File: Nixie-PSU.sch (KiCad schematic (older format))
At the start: 17 parts, among them J1 Conn_Mains, J2 Conn_Pwr_Out, Q1 MJE18008-D

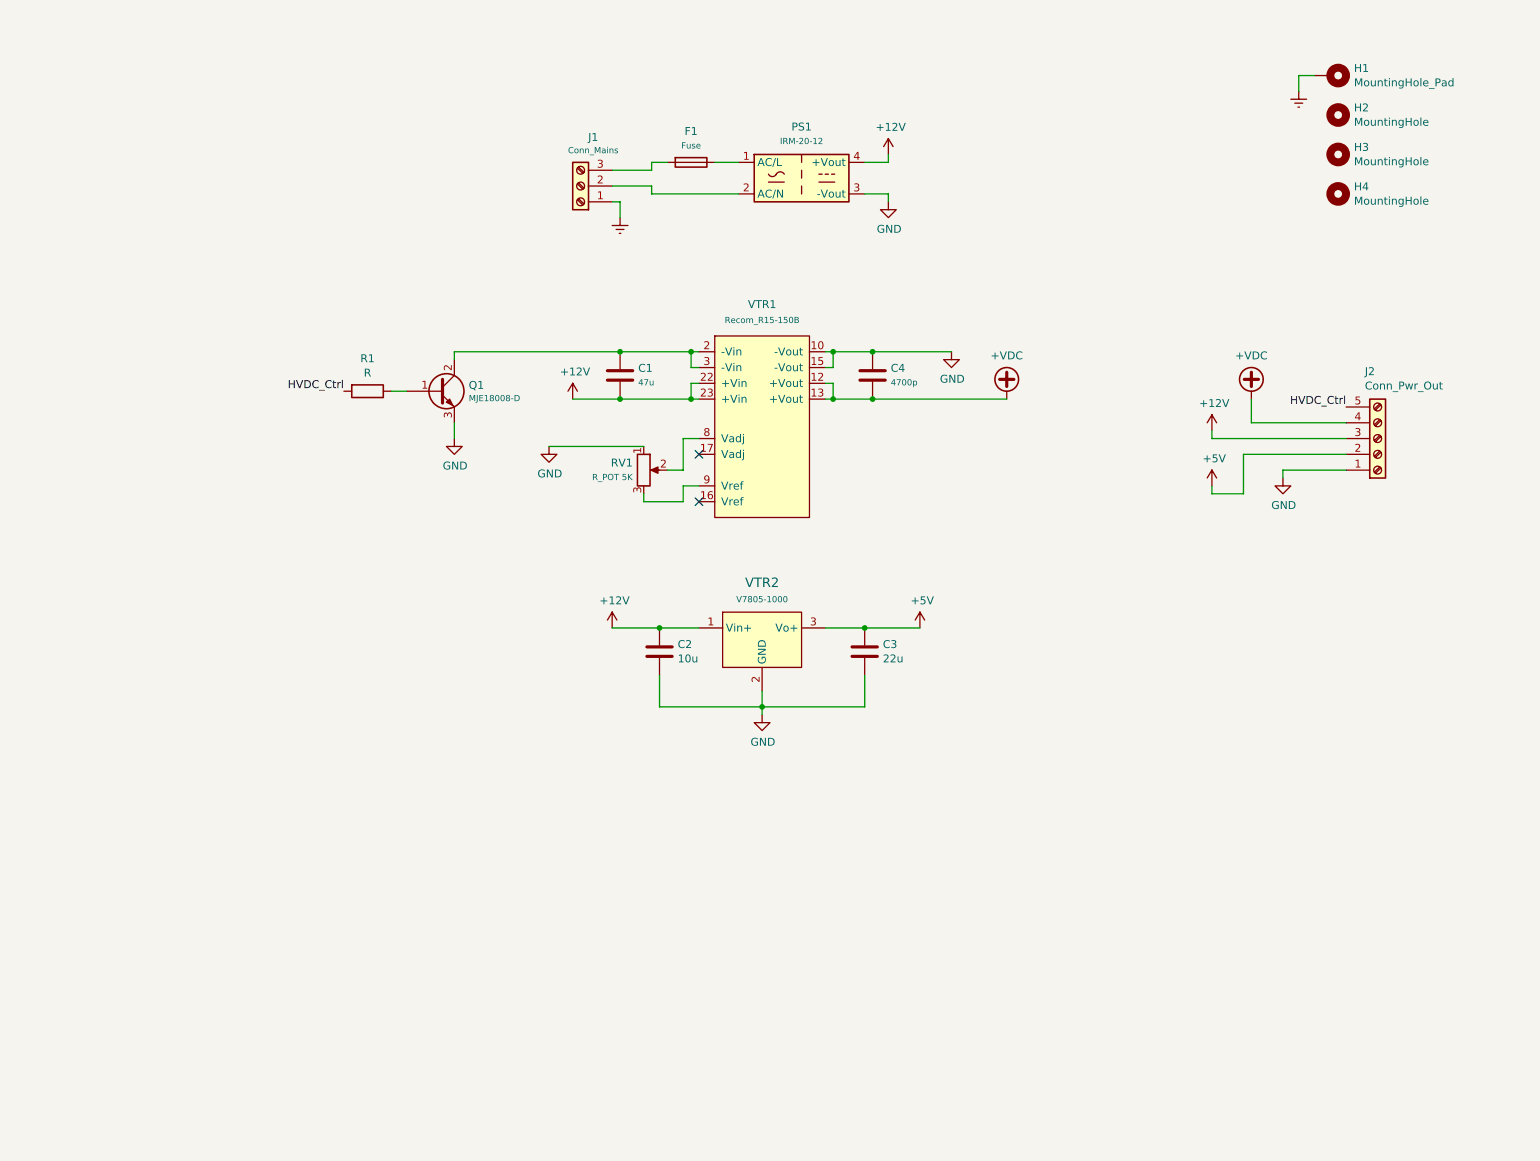
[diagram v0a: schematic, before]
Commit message: Cleaned-up docs slightly
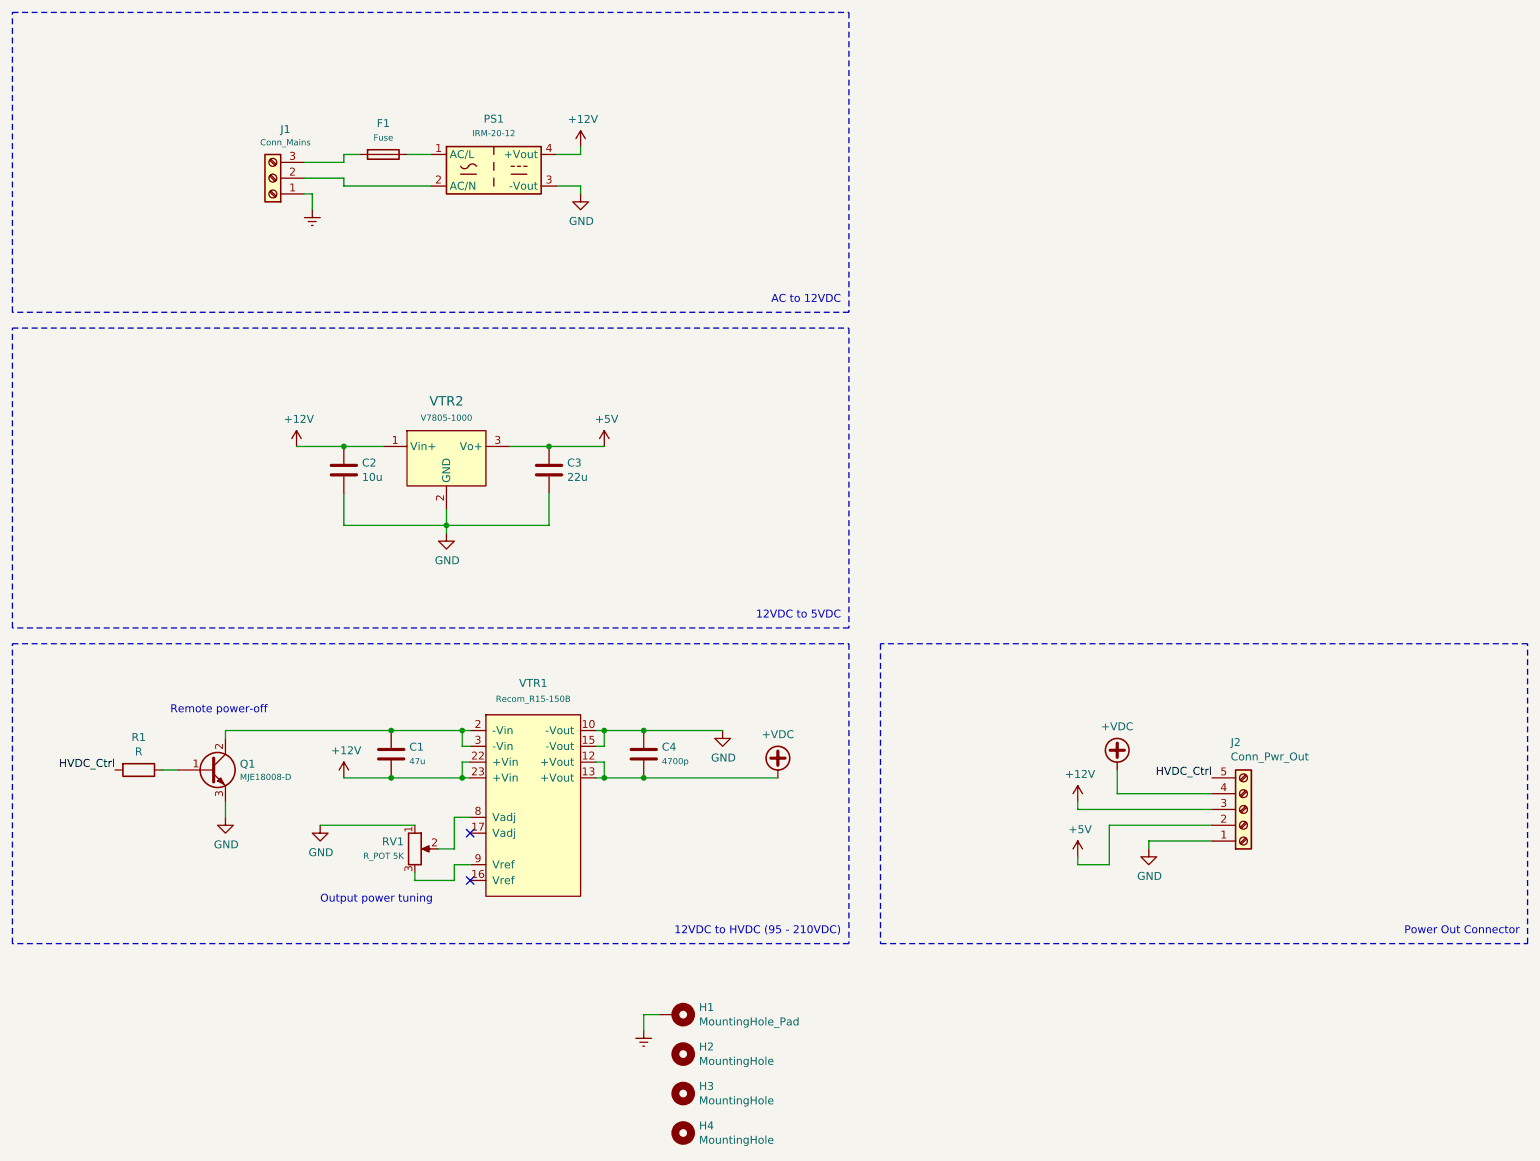
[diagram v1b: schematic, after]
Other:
- note added: "12VDC to 5VDC"
- note added: "12VDC to HVDC (95 - 210VDC)"
- note added: "AC to 12VDC"
- note added: "Output power tuning"
- note added: "Power Out Connector"
- note added: "Remote power-off"
- moved on the sheet: C1, C2, C3, C4, F1, H1, H2, H3, H4, J1, J2, PS1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
